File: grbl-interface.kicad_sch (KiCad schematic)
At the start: 12 parts, among them U6 ATmega328P-A

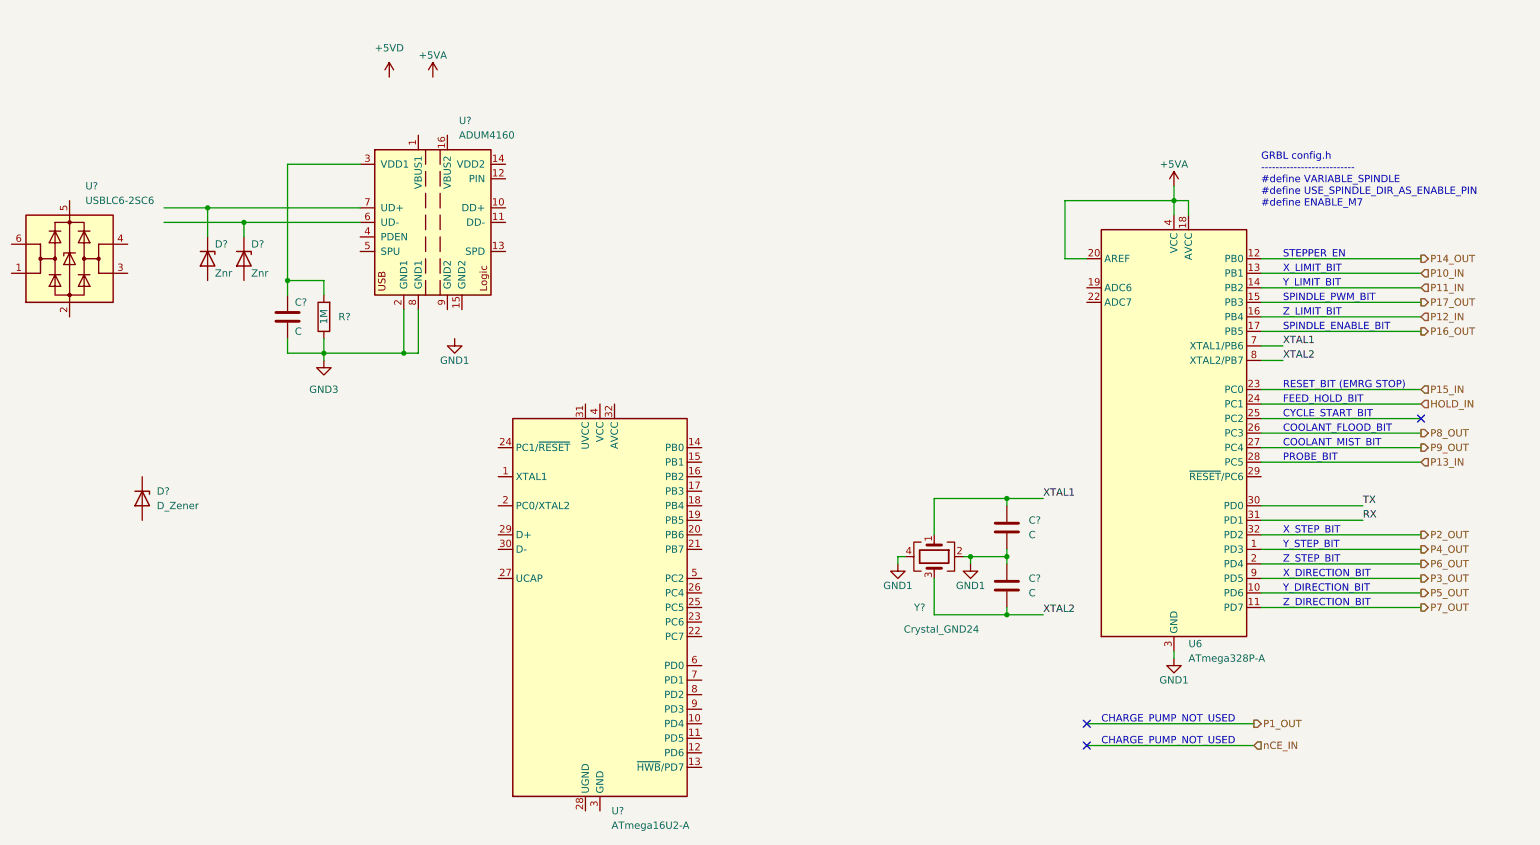
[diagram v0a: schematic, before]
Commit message: Optical isolator input current (10mA not 3mA) and wiring error fixed.
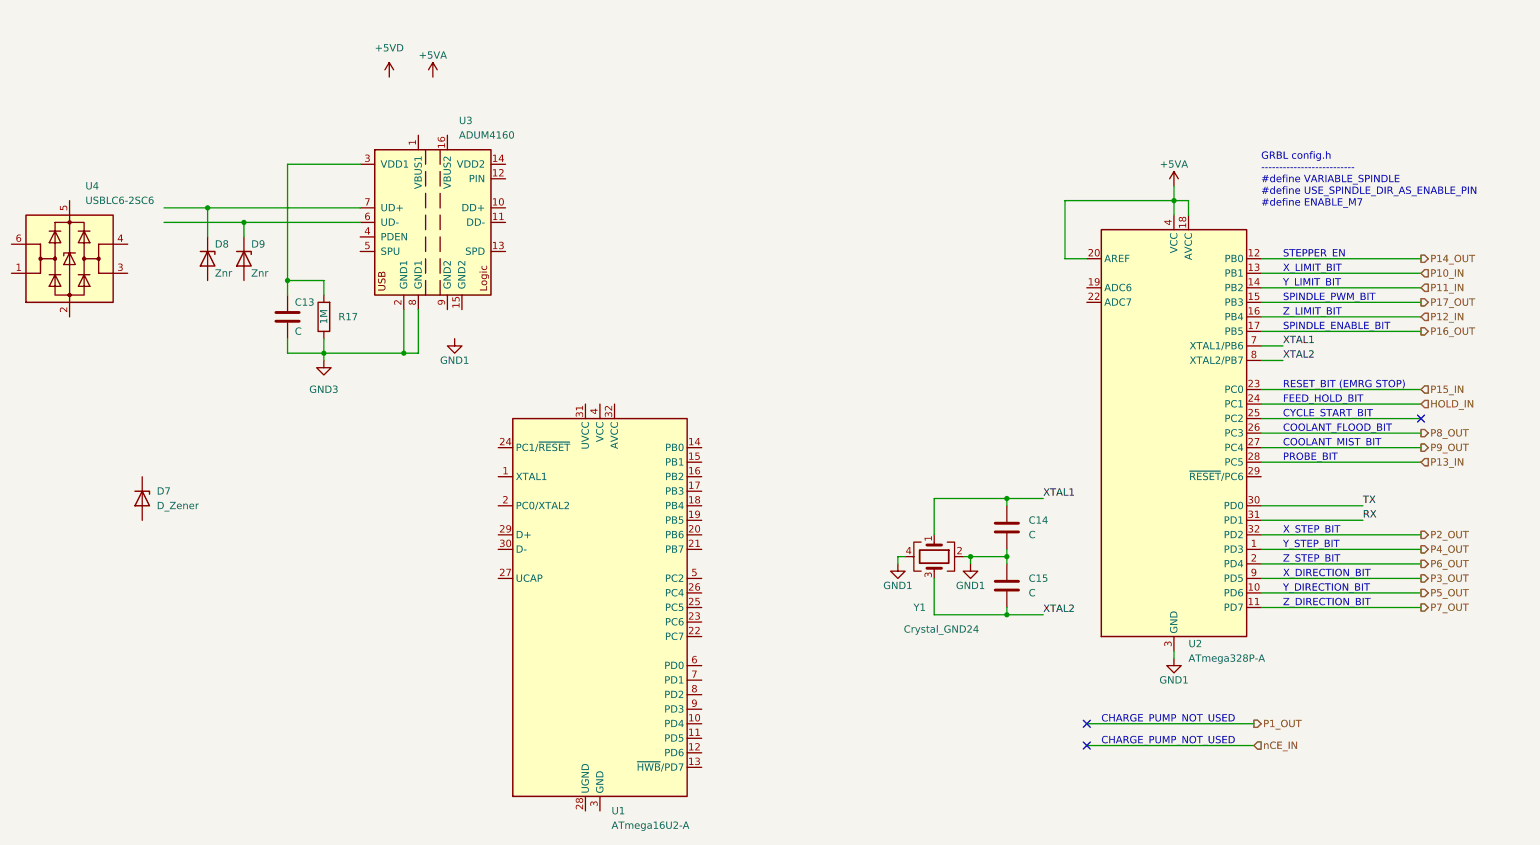
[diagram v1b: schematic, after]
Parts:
- gave numbers to parts that had none: 11
- renumbered U6 to U2
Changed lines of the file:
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@@
   (symbol (lib_id "Power_Protection:USBLC6-2SC6") (at 22.86 62.23 0) (unit 1)
     (in_bom yes) (on_board yes) (fields_autoplaced)
-    (property "Reference" "U?" (id 0) (at 25.6287 49.53 0)
+    (property "Reference" "U4" (id 0) (at 25.6287 49.53 0)
       (effects (font (size 1.27 1.27)) (justify left))
     )
@@
   (symbol (lib_id "Device:D_Zener") (at 35.56 104.14 270) (unit 1)
     (in_bom yes) (on_board yes) (fields_autoplaced)
-    (property "Reference" "D?" (id 0) (at 38.1 102.8699 90)
+    (property "Reference" "D7" (id 0) (at 38.1 102.8699 90)
       (effects (font (size 1.27 1.27)) (justify left))
     )
@@
   (symbol (lib_id "MCU_Microchip_ATmega:ATmega328P-A") (at 215.9 92.71 0) (unit 1)
     (in_bom yes) (on_board yes)
-    (property "Reference" "U6" (id 0) (at 218.44 129.54 0)
+    (property "Reference" "U2" (id 0) (at 218.44 129.54 0)
       (effects (font (size 1.27 1.27)) (justify left))
     )
@@
   (symbol (lib_id "Device:C") (at 60.96 72.39 0) (unit 1)
     (in_bom yes) (on_board yes)
-    (property "Reference" "C?" (id 0) (at 62.23 69.85 0)
+    (property "Reference" "C13" (id 0) (at 62.23 69.85 0)
       (effects (font (size 1.27 1.27)) (justify left))
     )
@@
   (symbol (lib_id "power:GND1") (at 90.17 76.2 0) (unit 1)
     (in_bom yes) (on_board yes)
-    (property "Reference" "#PWR?" (id 0) (at 90.17 82.55 0)
+    (property "Reference" "#PWR0157" (id 0) (at 90.17 82.55 0)
       (effects (font (size 1.27 1.27)) hide)
     )
@@
   (symbol (lib_id "Device:C") (at 186.69 109.22 0) (unit 1)
     (in_bom yes) (on_board yes) (fields_autoplaced)
-    (property "Reference" "C?" (id 0) (at 190.5 107.9499 0)
+    (property "Reference" "C14" (id 0) (at 190.5 107.9499 0)
       (effects (font (size 1.27 1.27)) (justify left))
     )
@@
   (symbol (lib_id "power:GND1") (at 180.34 115.57 0) (unit 1)
     (in_bom yes) (on_board yes)
-    (property "Reference" "#PWR?" (id 0) (at 180.34 121.92 0)
+    (property "Reference" "#PWR0158" (id 0) (at 180.34 121.92 0)
       (effects (font (size 1.27 1.27)) hide)
     )
@@
   (symbol (lib_id "Device:Crystal_GND24") (at 173.99 114.3 270) (unit 1)
     (in_bom yes) (on_board yes)
-    (property "Reference" "Y?" (id 0) (at 171.45 123.19 90))
+    (property "Reference" "Y1" (id 0) (at 171.45 123.19 90))
     (property "Value" "Crystal_GND24" (id 1) (at 175.26 127 90))
     (property "Footprint" "" (id 2) (at 173.99 114.3 0)
@@
   (symbol (lib_id "Device:D_Zener") (at 46.99 62.23 270) (unit 1)
     (in_bom yes) (on_board yes)
-    (property "Reference" "D?" (id 0) (at 48.26 59.69 90)
+    (property "Reference" "D8" (id 0) (at 48.26 59.69 90)
       (effects (font (size 1.27 1.27)) (justify left))
     )
@@
   (symbol (lib_id "power:GND1") (at 167.64 115.57 0) (unit 1)
     (in_bom yes) (on_board yes)
-    (property "Reference" "#PWR?" (id 0) (at 167.64 121.92 0)
+    (property "Reference" "#PWR0153" (id 0) (at 167.64 121.92 0)
       (effects (font (size 1.27 1.27)) hide)
     )
@@
   (symbol (lib_id "MCU_Microchip_ATmega:ATmega16U2-A") (at 115.57 123.19 0) (unit 1)
     (in_bom yes) (on_board yes) (fields_autoplaced)
-    (property "Reference" "U?" (id 0) (at 117.5894 158.75 0)
+    (property "Reference" "U1" (id 0) (at 117.5894 158.75 0)
       (effects (font (size 1.27 1.27)) (justify left))
     )
@@
   (symbol (lib_id "power:+5VA") (at 86.36 30.48 0) (unit 1)
     (in_bom yes) (on_board yes)
-    (property "Reference" "#PWR?" (id 0) (at 86.36 34.29 0)
+    (property "Reference" "#PWR0156" (id 0) (at 86.36 34.29 0)
       (effects (font (size 1.27 1.27)) hide)
     )
@@
   (symbol (lib_id "Device:C") (at 186.69 119.38 0) (unit 1)
     (in_bom yes) (on_board yes) (fields_autoplaced)
-    (property "Reference" "C?" (id 0) (at 190.5 118.1099 0)
+    (property "Reference" "C15" (id 0) (at 190.5 118.1099 0)
       (effects (font (size 1.27 1.27)) (justify left))
     )
@@
   (symbol (lib_id "power:+5VD") (at 78.74 30.48 0) (unit 1)
     (in_bom yes) (on_board yes) (fields_autoplaced)
-    (property "Reference" "#PWR?" (id 0) (at 78.74 34.29 0)
+    (property "Reference" "#PWR0155" (id 0) (at 78.74 34.29 0)
       (effects (font (size 1.27 1.27)) hide)
     )
@@
   (symbol (lib_id "Device:R") (at 67.31 72.39 180) (unit 1)
     (in_bom yes) (on_board yes)
-    (property "Reference" "R?" (id 0) (at 69.85 72.39 0)
+    (property "Reference" "R17" (id 0) (at 69.85 72.39 0)
       (effects (font (size 1.27 1.27)) (justify right))
     )
@@
   (symbol (lib_id "Interface_USB:ADUM4160") (at 86.36 55.88 0) (unit 1)
     (in_bom yes) (on_board yes) (fields_autoplaced)
-    (property "Reference" "U?" (id 0) (at 90.9194 38.1 0)
+    (property "Reference" "U3" (id 0) (at 90.9194 38.1 0)
       (effects (font (size 1.27 1.27)) (justify left))
     )
@@
   (symbol (lib_id "Device:D_Zener") (at 53.34 62.23 270) (unit 1)
     (in_bom yes) (on_board yes)
-    (property "Reference" "D?" (id 0) (at 54.61 59.69 90)
+    (property "Reference" "D9" (id 0) (at 54.61 59.69 90)
       (effects (font (size 1.27 1.27)) (justify left))
     )
@@
   (symbol (lib_id "power:GND3") (at 67.31 80.01 0) (unit 1)
     (in_bom yes) (on_board yes) (fields_autoplaced)
-    (property "Reference" "#PWR?" (id 0) (at 67.31 86.36 0)
-      (effects (font (size 1.27 1.27)) hide)
-    )
+    (property "Reference" "#PWR0154" (id 0) (at 67.31 86.36 0)
+      (effects (font (size 1.27 1.27)) hide)
+    )

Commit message: Multiple flaws resolved
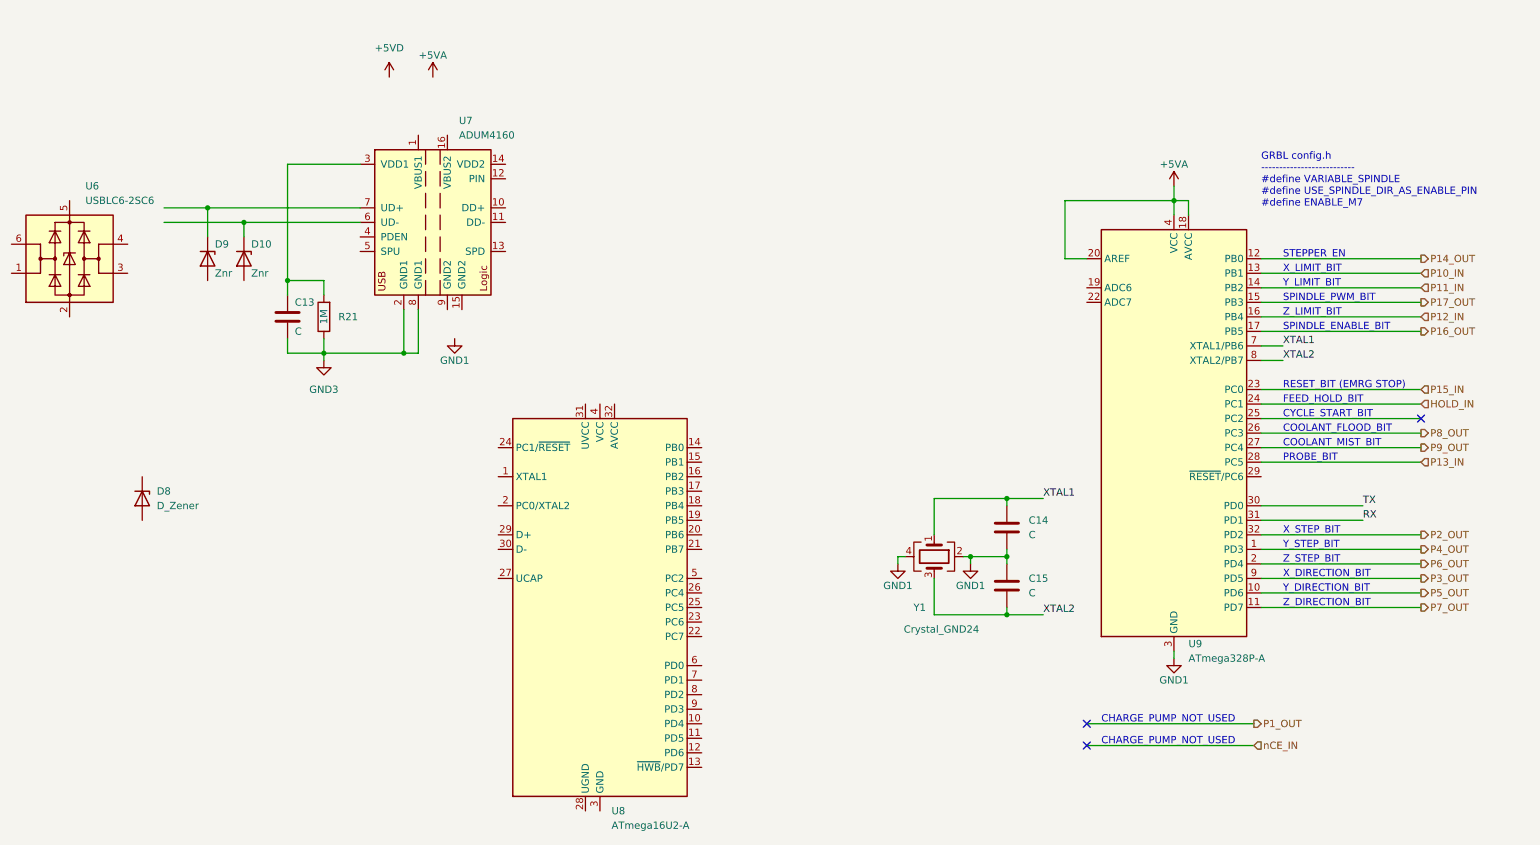
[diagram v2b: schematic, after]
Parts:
- renumbered D9 to D10, D7 to D8, D8 to D9, R17 to R21, U4 to U6, U3 to U7, U1 to U8, U2 to U9
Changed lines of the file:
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@@
   (symbol (lib_id "Power_Protection:USBLC6-2SC6") (at 22.86 62.23 0) (unit 1)
     (in_bom yes) (on_board yes) (fields_autoplaced)
-    (property "Reference" "U4" (id 0) (at 25.6287 49.53 0)
+    (property "Reference" "U6" (id 0) (at 25.6287 49.53 0)
       (effects (font (size 1.27 1.27)) (justify left))
     )
@@
   (symbol (lib_id "Device:D_Zener") (at 35.56 104.14 270) (unit 1)
     (in_bom yes) (on_board yes) (fields_autoplaced)
-    (property "Reference" "D7" (id 0) (at 38.1 102.8699 90)
+    (property "Reference" "D8" (id 0) (at 38.1 102.8699 90)
       (effects (font (size 1.27 1.27)) (justify left))
     )
@@
   (symbol (lib_id "MCU_Microchip_ATmega:ATmega328P-A") (at 215.9 92.71 0) (unit 1)
     (in_bom yes) (on_board yes)
-    (property "Reference" "U2" (id 0) (at 218.44 129.54 0)
+    (property "Reference" "U9" (id 0) (at 218.44 129.54 0)
       (effects (font (size 1.27 1.27)) (justify left))
     )
@@
   (symbol (lib_id "power:GND1") (at 90.17 76.2 0) (unit 1)
     (in_bom yes) (on_board yes)
-    (property "Reference" "#PWR0157" (id 0) (at 90.17 82.55 0)
+    (property "Reference" "#PWR087" (id 0) (at 90.17 82.55 0)
       (effects (font (size 1.27 1.27)) hide)
     )
@@
   (symbol (lib_id "power:GND1") (at 180.34 115.57 0) (unit 1)
     (in_bom yes) (on_board yes)
-    (property "Reference" "#PWR0158" (id 0) (at 180.34 121.92 0)
+    (property "Reference" "#PWR089" (id 0) (at 180.34 121.92 0)
       (effects (font (size 1.27 1.27)) hide)
     )
@@
   (symbol (lib_id "Device:D_Zener") (at 46.99 62.23 270) (unit 1)
     (in_bom yes) (on_board yes)
-    (property "Reference" "D8" (id 0) (at 48.26 59.69 90)
+    (property "Reference" "D9" (id 0) (at 48.26 59.69 90)
       (effects (font (size 1.27 1.27)) (justify left))
     )
@@
   (symbol (lib_id "power:GND1") (at 167.64 115.57 0) (unit 1)
     (in_bom yes) (on_board yes)
-    (property "Reference" "#PWR0153" (id 0) (at 167.64 121.92 0)
+    (property "Reference" "#PWR088" (id 0) (at 167.64 121.92 0)
       (effects (font (size 1.27 1.27)) hide)
     )
@@
   (symbol (lib_id "MCU_Microchip_ATmega:ATmega16U2-A") (at 115.57 123.19 0) (unit 1)
     (in_bom yes) (on_board yes) (fields_autoplaced)
-    (property "Reference" "U1" (id 0) (at 117.5894 158.75 0)
+    (property "Reference" "U8" (id 0) (at 117.5894 158.75 0)
       (effects (font (size 1.27 1.27)) (justify left))
     )
@@
   (symbol (lib_id "power:+5VA") (at 86.36 30.48 0) (unit 1)
     (in_bom yes) (on_board yes)
-    (property "Reference" "#PWR0156" (id 0) (at 86.36 34.29 0)
+    (property "Reference" "#PWR086" (id 0) (at 86.36 34.29 0)
       (effects (font (size 1.27 1.27)) hide)
     )
@@
   (symbol (lib_id "power:+5VD") (at 78.74 30.48 0) (unit 1)
     (in_bom yes) (on_board yes) (fields_autoplaced)
-    (property "Reference" "#PWR0155" (id 0) (at 78.74 34.29 0)
+    (property "Reference" "#PWR085" (id 0) (at 78.74 34.29 0)
       (effects (font (size 1.27 1.27)) hide)
     )
@@
   (symbol (lib_id "power:GND1") (at 215.9 132.08 0) (unit 1)
     (in_bom yes) (on_board yes)
-    (property "Reference" "#PWR0152" (id 0) (at 215.9 138.43 0)
+    (property "Reference" "#PWR091" (id 0) (at 215.9 138.43 0)
       (effects (font (size 1.27 1.27)) hide)
     )
@@
   (symbol (lib_id "Device:R") (at 67.31 72.39 180) (unit 1)
     (in_bom yes) (on_board yes)
-    (property "Reference" "R17" (id 0) (at 69.85 72.39 0)
+    (property "Reference" "R21" (id 0) (at 69.85 72.39 0)
       (effects (font (size 1.27 1.27)) (justify right))
     )
@@
   (symbol (lib_id "power:+5VA") (at 215.9 49.53 0) (unit 1)
     (in_bom yes) (on_board yes)
-    (property "Reference" "#PWR0151" (id 0) (at 215.9 53.34 0)
+    (property "Reference" "#PWR090" (id 0) (at 215.9 53.34 0)
       (effects (font (size 1.27 1.27)) hide)
     )
@@
   (symbol (lib_id "Interface_USB:ADUM4160") (at 86.36 55.88 0) (unit 1)
     (in_bom yes) (on_board yes) (fields_autoplaced)
-    (property "Reference" "U3" (id 0) (at 90.9194 38.1 0)
+    (property "Reference" "U7" (id 0) (at 90.9194 38.1 0)
       (effects (font (size 1.27 1.27)) (justify left))
     )
@@
   (symbol (lib_id "Device:D_Zener") (at 53.34 62.23 270) (unit 1)
     (in_bom yes) (on_board yes)
-    (property "Reference" "D9" (id 0) (at 54.61 59.69 90)
+    (property "Reference" "D10" (id 0) (at 54.61 59.69 90)
       (effects (font (size 1.27 1.27)) (justify left))
     )
@@
   (symbol (lib_id "power:GND3") (at 67.31 80.01 0) (unit 1)
     (in_bom yes) (on_board yes) (fields_autoplaced)
-    (property "Reference" "#PWR0154" (id 0) (at 67.31 86.36 0)
-      (effects (font (size 1.27 1.27)) hide)
-    )
+    (property "Reference" "#PWR084" (id 0) (at 67.31 86.36 0)
+      (effects (font (size 1.27 1.27)) hide)
+    )

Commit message: wip
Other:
- moved on the sheet: C13, D10, D8, D9, R21, U6, U7
